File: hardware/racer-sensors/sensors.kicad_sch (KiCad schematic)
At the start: 14 parts, among them J1 Conn_02x03_SMT, U1 OPT4060DTSR, U2 HAL1501SU-A

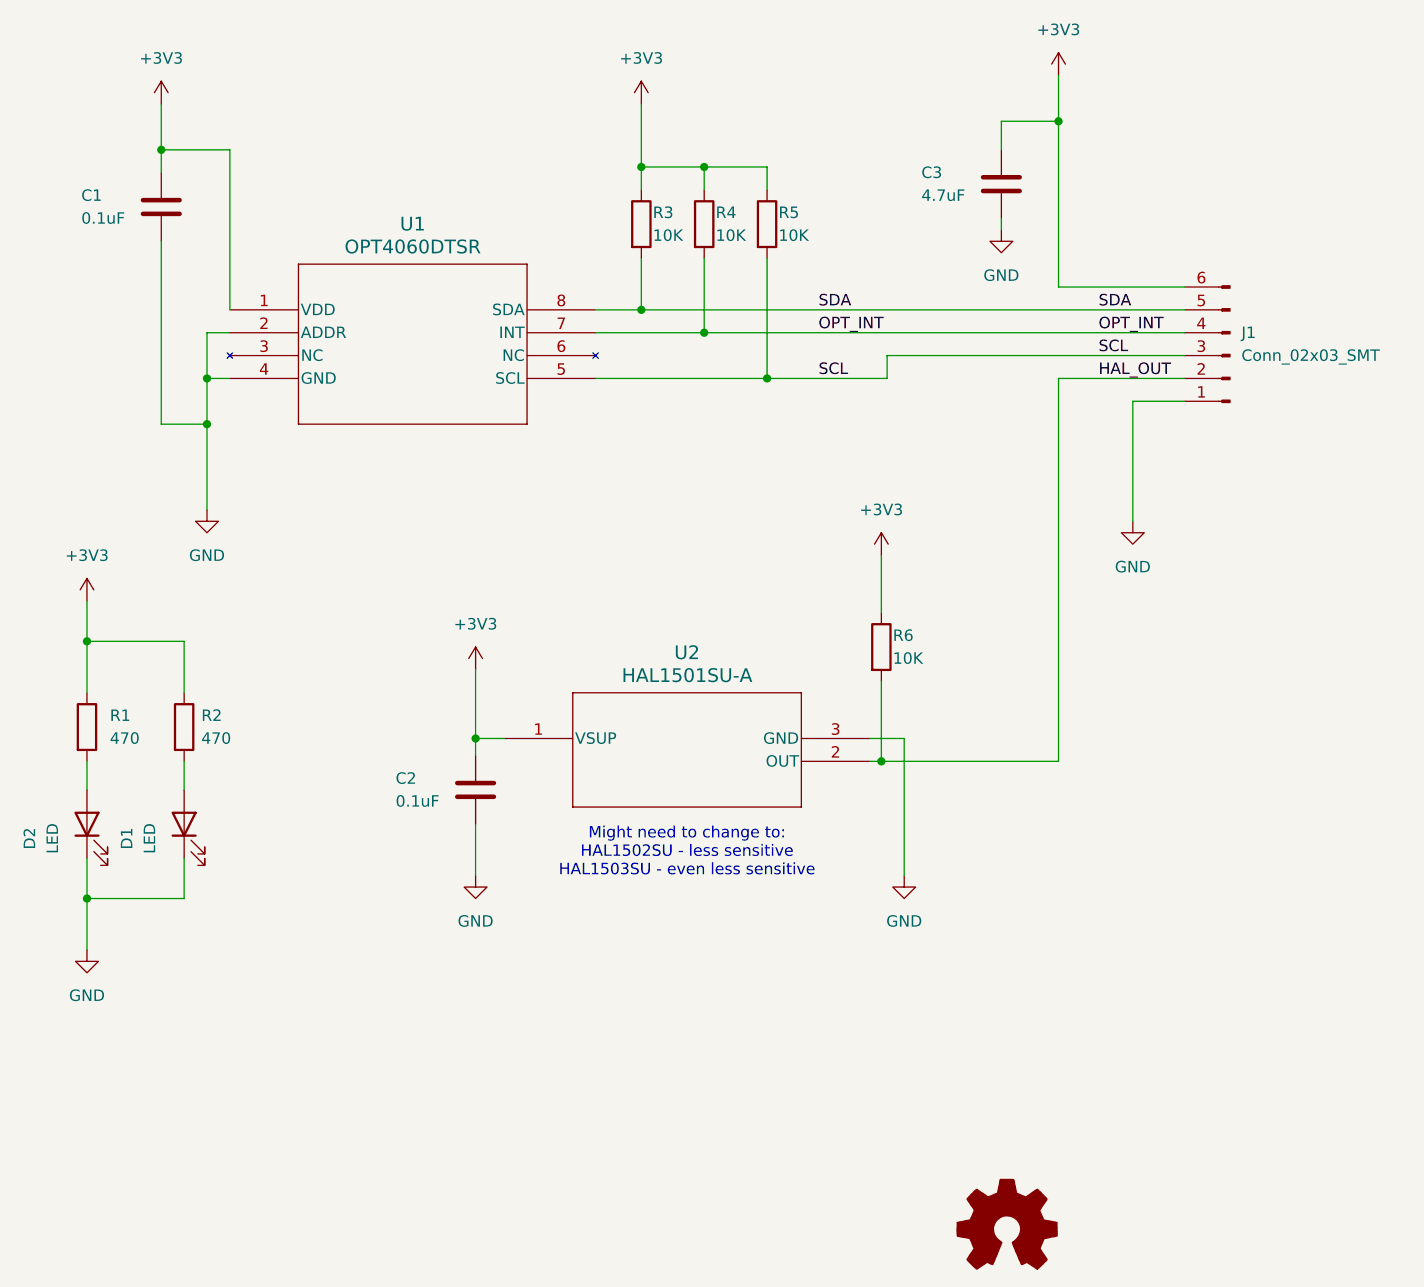
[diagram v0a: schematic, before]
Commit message: Schematic readability update
Updated Schematics to hierarchical, Schematic size to A4.
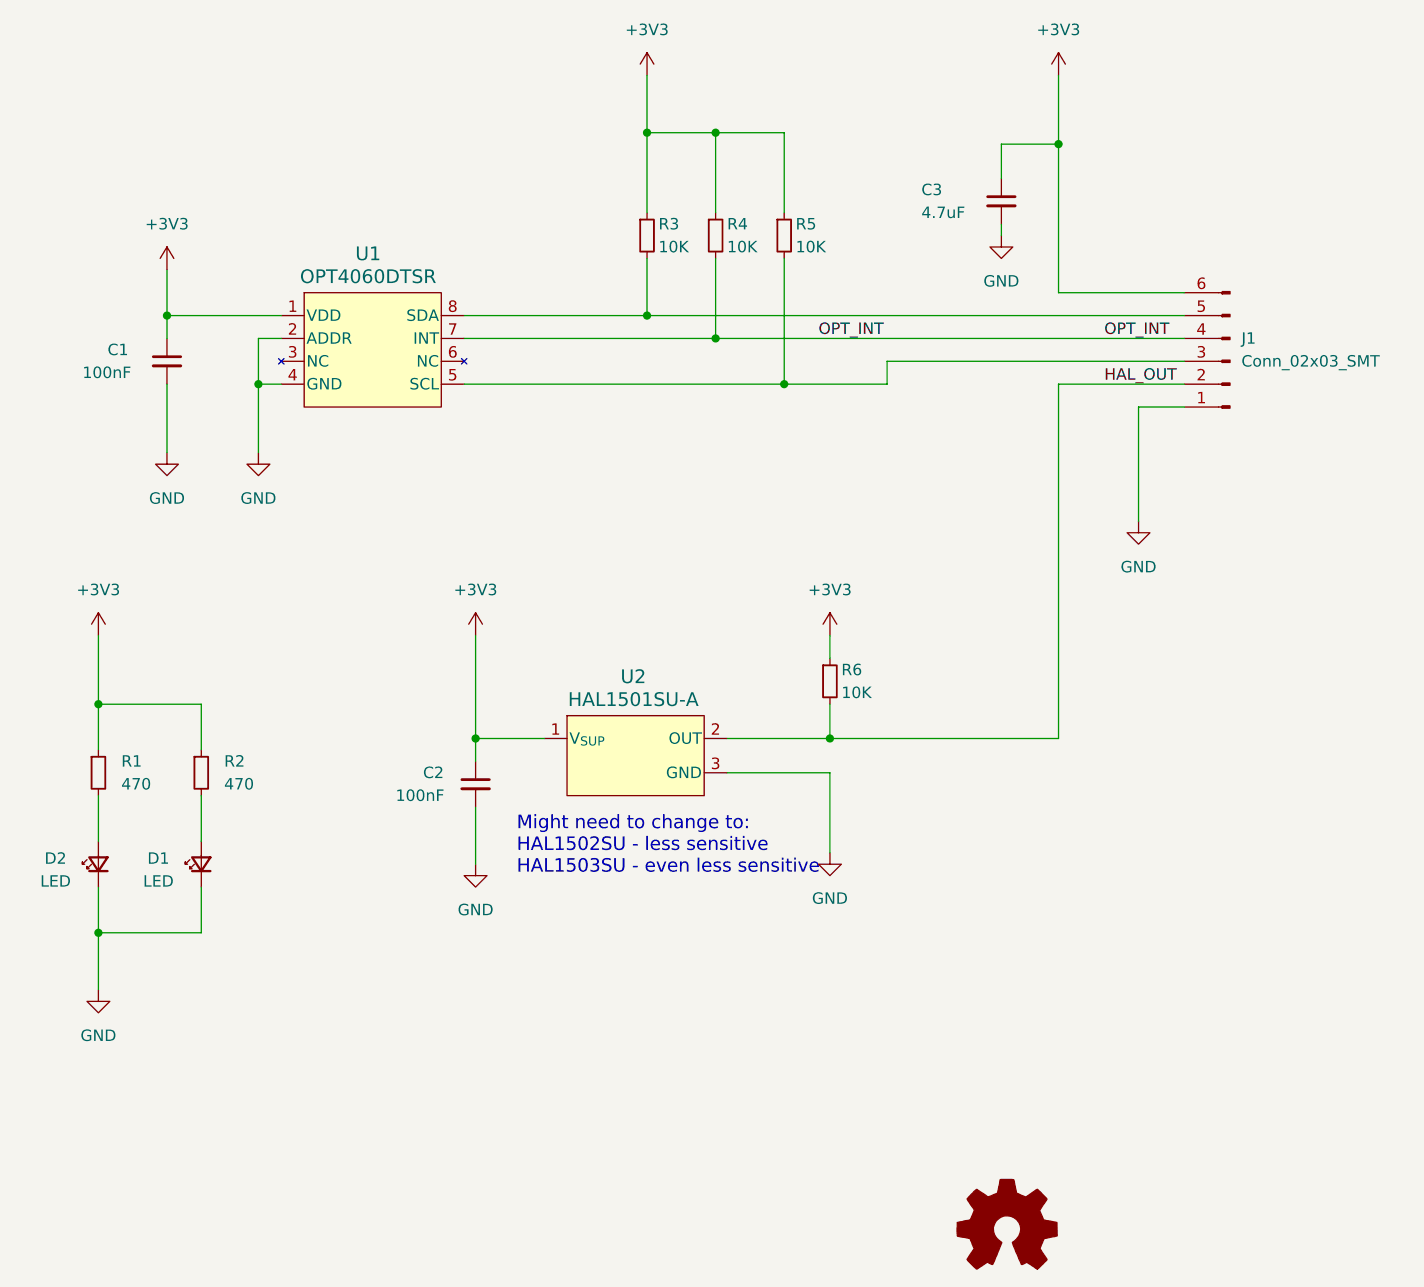
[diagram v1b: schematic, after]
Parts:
- C1, C2: value 0.1uF -> 100nF; symbol Device:C -> Device:C_Small
- C3: symbol Device:C -> Device:C_Small
- D1, D2: symbol Device:LED -> Device:LED_Small
- R1, R2, R3, R4, R5, R6: symbol Device:R -> Device:R_Small
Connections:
- net SCL: no longer names the net of J1.3 (Pin_3), R5.2, U1.5 (SCL)
- net SDA: no longer names the net of J1.5 (Pin_5), R3.2, U1.8 (SDA)
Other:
- moved on the sheet: C1, C2, C3, D1, D2, J1, R1, R2, R3, R4, R5, R6
